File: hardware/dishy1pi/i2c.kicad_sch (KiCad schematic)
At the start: 19 parts, among them CN4 KF2EDGR-2.54-4P, CN5 KF2EDGR-2.54-4P, U6 LTC4311ISC6#TRPBF, U7 ISO1540DR, U8 LM75BIMX-5/NOPB

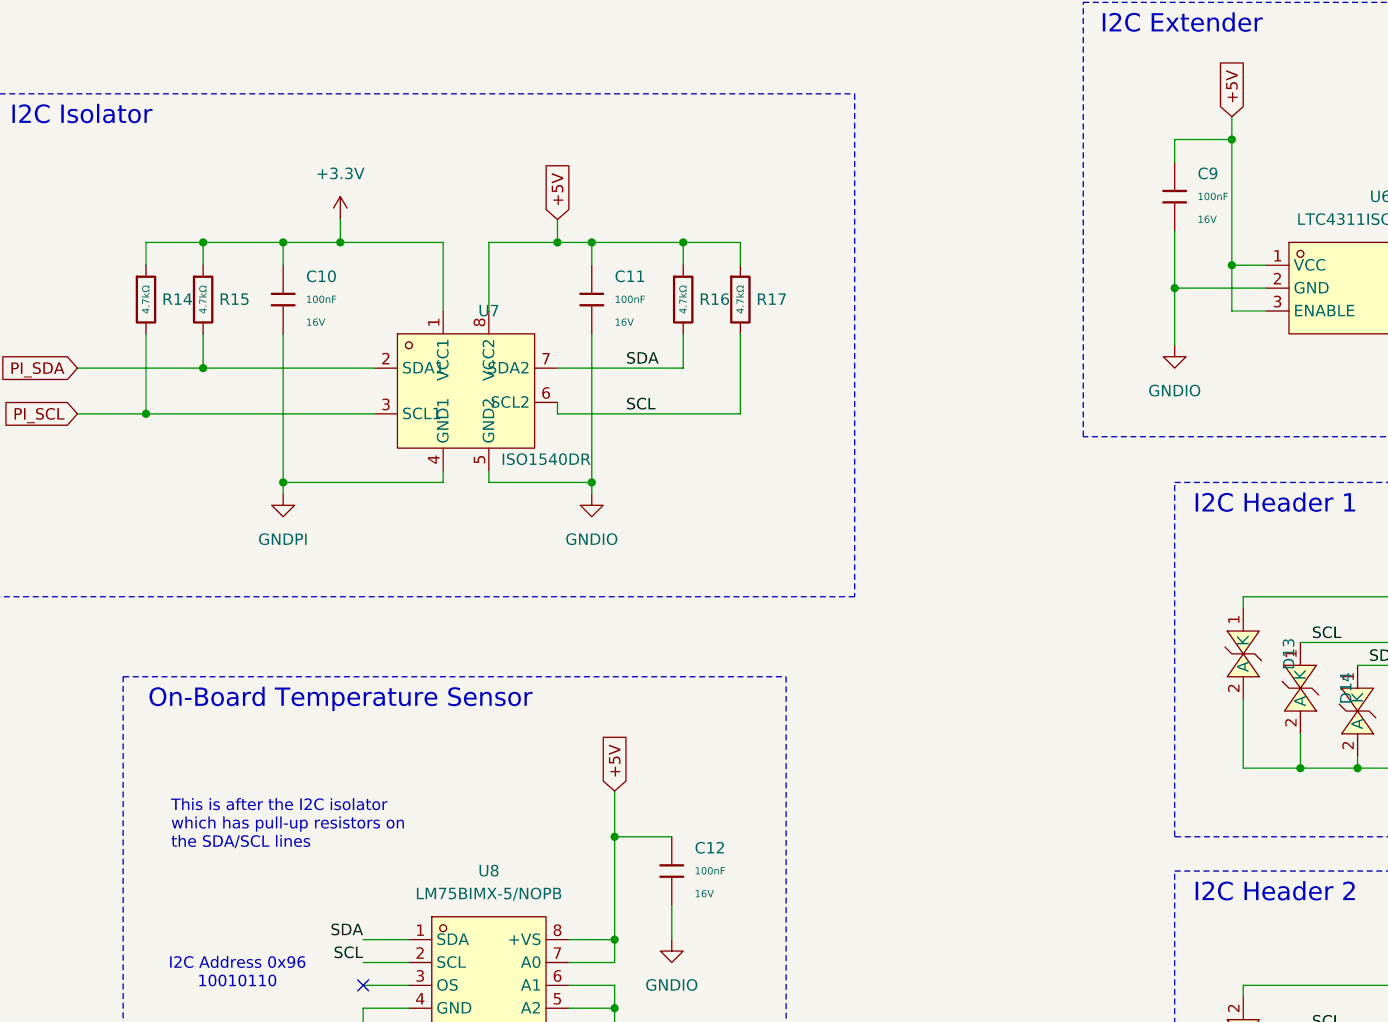
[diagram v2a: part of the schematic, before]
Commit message: Modifications based on first board assembly
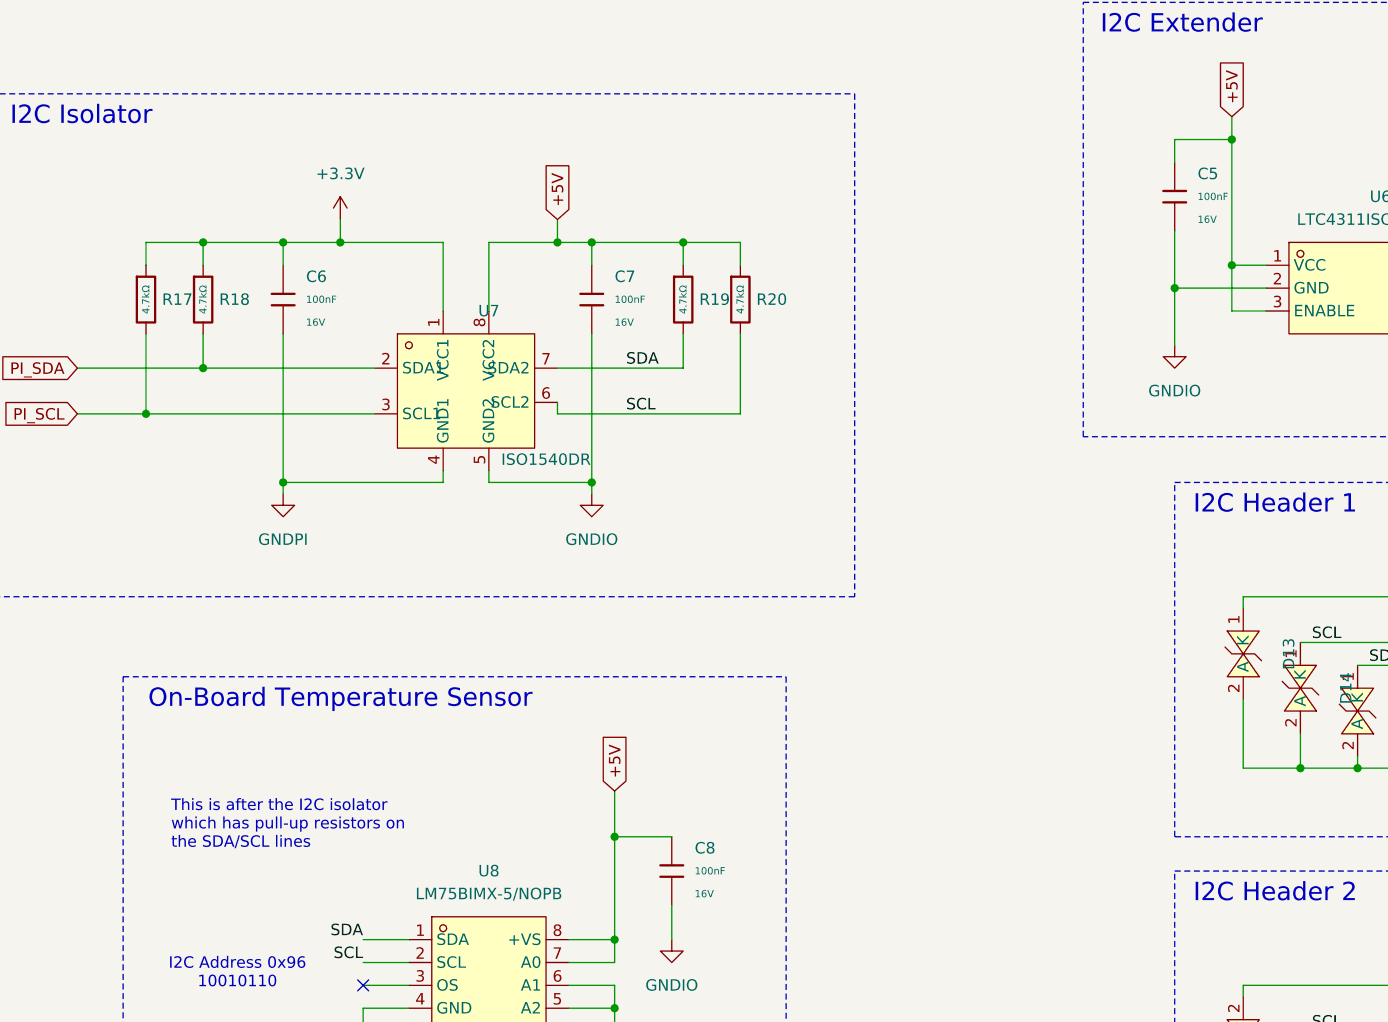
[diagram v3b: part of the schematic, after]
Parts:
- renumbered C9 to C5, C10 to C6, C11 to C7, C12 to C8, R14 to R17, R15 to R18, R16 to R19, R17 to R20
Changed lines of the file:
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@@
 		(title "I2C")
 		(date "2025-09-28")
-		(rev "1.1")
+		(rev "1.2")
 		(company "JRDish")
 		(comment 1 "I2C Circuits")
@@
 		(dnp no)
 		(fields_autoplaced yes)
-		(property "Reference" "C12"
+		(property "Reference" "C8"
 			(at 116.84 120.6499 0)
 			(effects
@@
 			(project ""
 				(path "/e63e39d7-6ac0-4ffd-8aa3-1841a4541b55/2849b2fb-7367-47ef-9d93-b400c9666642"
-					(reference "C12")
+					(reference "C8")
 					(unit 1)
 				)
@@
 		(on_board yes)
 		(dnp no)
-		(property "Reference" "R15"
+		(property "Reference" "R18"
 			(at 64.008 59.69 0)
 			(effects
@@
 			(project "DishyPi1"
 				(path "/e63e39d7-6ac0-4ffd-8aa3-1841a4541b55/2849b2fb-7367-47ef-9d93-b400c9666642"
-					(reference "R15")
+					(reference "R18")
 					(unit 1)
 				)
@@
 		(dnp no)
 		(fields_autoplaced yes)
-		(property "Reference" "#PWR25"
+		(property "Reference" "#PWR023"
 			(at 114.3 137.16 0)
 			(effects
@@
 			(project "DishyPi1"
 				(path "/e63e39d7-6ac0-4ffd-8aa3-1841a4541b55/2849b2fb-7367-47ef-9d93-b400c9666642"
-					(reference "#PWR25")
+					(reference "#PWR023")
 					(unit 1)
 				)
@@
 		(dnp no)
 		(fields_autoplaced yes)
-		(property "Reference" "#PWR23"
+		(property "Reference" "#PWR021"
 			(at 105.41 87.63 0)
 			(effects
@@
 			(project ""
 				(path "/e63e39d7-6ac0-4ffd-8aa3-1841a4541b55/2849b2fb-7367-47ef-9d93-b400c9666642"
-					(reference "#PWR23")
+					(reference "#PWR021")
 					(unit 1)
 				)
@@
 		(dnp no)
 		(fields_autoplaced yes)
-		(property "Reference" "C9"
+		(property "Reference" "C5"
 			(at 172.72 45.7199 0)
 			(effects
@@
 			(project "DishyPi1"
 				(path "/e63e39d7-6ac0-4ffd-8aa3-1841a4541b55/2849b2fb-7367-47ef-9d93-b400c9666642"
-					(reference "C9")
+					(reference "C5")
 					(unit 1)
 				)
@@
 		(dnp no)
 		(fields_autoplaced yes)
-		(property "Reference" "#PWR21"
+		(property "Reference" "#PWR019"
 			(at 208.28 71.12 0)
 			(effects
@@
 			(project "DishyPi1"
 				(path "/e63e39d7-6ac0-4ffd-8aa3-1841a4541b55/2849b2fb-7367-47ef-9d93-b400c9666642"
-					(reference "#PWR21")
+					(reference "#PWR019")
 					(unit 1)
 				)
@@
 		(dnp no)
 		(fields_autoplaced yes)
-		(property "Reference" "#PWR19"
+		(property "Reference" "#PWR017"
 			(at 77.47 54.61 0)
 			(effects
@@
 			(project ""
 				(path "/e63e39d7-6ac0-4ffd-8aa3-1841a4541b55/2849b2fb-7367-47ef-9d93-b400c9666642"
-					(reference "#PWR19")
+					(reference "#PWR017")
 					(unit 1)
 				)
@@
 		(on_board yes)
 		(dnp no)
-		(property "Reference" "R14"
+		(property "Reference" "R17"
 			(at 57.658 59.69 0)
 			(effects
@@
 			(project "DishyPi1"
 				(path "/e63e39d7-6ac0-4ffd-8aa3-1841a4541b55/2849b2fb-7367-47ef-9d93-b400c9666642"
-					(reference "R14")
+					(reference "R17")
 					(unit 1)
 				)
@@
 		(on_board yes)
 		(dnp no)
-		(property "Reference" "#PWR24"
+		(property "Reference" "#PWR022"
 			(at 196.85 119.38 0)
 			(effects
@@
 			(project ""
 				(path "/e63e39d7-6ac0-4ffd-8aa3-1841a4541b55/2849b2fb-7367-47ef-9d93-b400c9666642"
-					(reference "#PWR24")
+					(reference "#PWR022")
 					(unit 1)
 				)
@@
 		(dnp no)
 		(fields_autoplaced yes)
-		(property "Reference" "#PWR20"
+		(property "Reference" "#PWR018"
 			(at 170.18 71.12 0)
 			(effects
@@
 			(project "DishyPi1"
 				(path "/e63e39d7-6ac0-4ffd-8aa3-1841a4541b55/2849b2fb-7367-47ef-9d93-b400c9666642"
-					(reference "#PWR20")
+					(reference "#PWR018")
 					(unit 1)
 				)
@@
 		(on_board yes)
 		(dnp no)
-		(property "Reference" "R17"
+		(property "Reference" "R20"
 			(at 123.698 59.69 0)
 			(effects
@@
 			(project "DishyPi1"
 				(path "/e63e39d7-6ac0-4ffd-8aa3-1841a4541b55/2849b2fb-7367-47ef-9d93-b400c9666642"
-					(reference "R17")
+					(reference "R20")
 					(unit 1)
 				)
@@
 		(dnp no)
 		(fields_autoplaced yes)
-		(property "Reference" "C10"
+		(property "Reference" "C6"
 			(at 73.66 57.1499 0)
 			(effects
@@
 			(project ""
 				(path "/e63e39d7-6ac0-4ffd-8aa3-1841a4541b55/2849b2fb-7367-47ef-9d93-b400c9666642"
-					(reference "C10")
+					(reference "C6")
 					(unit 1)
 				)
@@
 		(on_board yes)
 		(dnp no)
-		(property "Reference" "R16"
+		(property "Reference" "R19"
 			(at 117.348 59.69 0)
 			(effects
@@
 			(project ""
 				(path "/e63e39d7-6ac0-4ffd-8aa3-1841a4541b55/2849b2fb-7367-47ef-9d93-b400c9666642"
-					(reference "R16")
+					(reference "R19")
 					(unit 1)
 				)
@@
 		(dnp no)
 		(fields_autoplaced yes)
-		(property "Reference" "#PWR22"
+		(property "Reference" "#PWR020"
 			(at 71.12 87.63 0)
 			(effects
@@
 			(project ""
 				(path "/e63e39d7-6ac0-4ffd-8aa3-1841a4541b55/2849b2fb-7367-47ef-9d93-b400c9666642"
-					(reference "#PWR22")
+					(reference "#PWR020")
 					(unit 1)
 				)
@@
 		(dnp no)
 		(fields_autoplaced yes)
-		(property "Reference" "C11"
+		(property "Reference" "C7"
 			(at 107.95 57.1499 0)
 			(effects
@@
 			(project "DishyPi1"
 				(path "/e63e39d7-6ac0-4ffd-8aa3-1841a4541b55/2849b2fb-7367-47ef-9d93-b400c9666642"
-					(reference "C11")
+					(reference "C7")
 					(unit 1)
 				)
@@
 		(on_board yes)
 		(dnp no)
-		(property "Reference" "#PWR27"
+		(property "Reference" "#PWR025"
 			(at 196.85 162.56 0)
 			(effects
@@
 			(project "DishyPi1"
 				(path "/e63e39d7-6ac0-4ffd-8aa3-1841a4541b55/2849b2fb-7367-47ef-9d93-b400c9666642"
-					(reference "#PWR27")
+					(reference "#PWR025")
 					(unit 1)
 				)
@@
 		(dnp no)
 		(fields_autoplaced yes)
-		(property "Reference" "#PWR26"
+		(property "Reference" "#PWR024"
 			(at 93.98 156.21 0)
 			(effects
@@
 			(project "DishyPi1"
 				(path "/e63e39d7-6ac0-4ffd-8aa3-1841a4541b55/2849b2fb-7367-47ef-9d93-b400c9666642"
-					(reference "#PWR26")
+					(reference "#PWR024")
 					(unit 1)
 				)

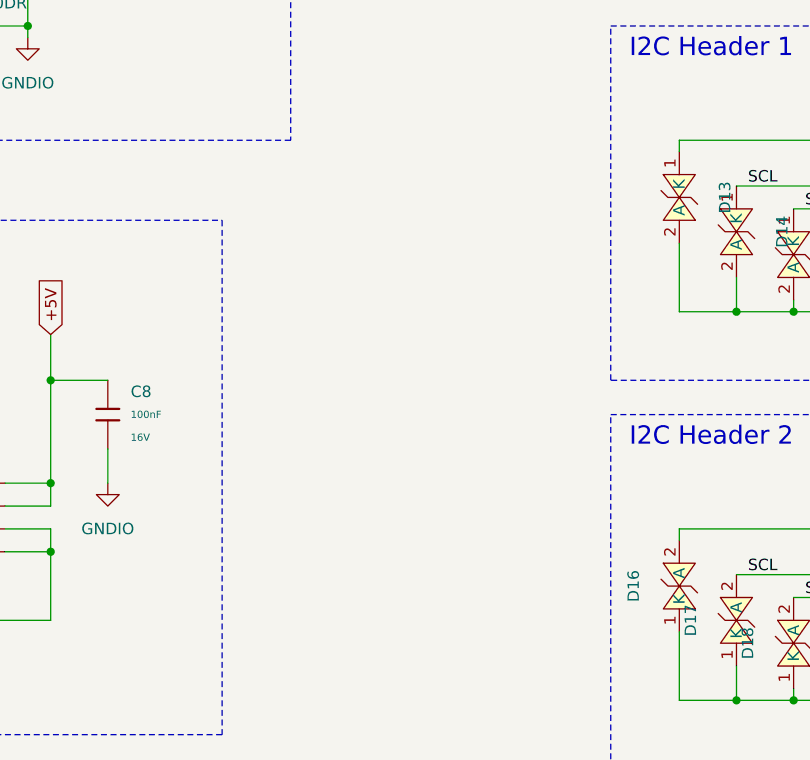
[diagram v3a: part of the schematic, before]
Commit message: Added power circuit to dishy schematic
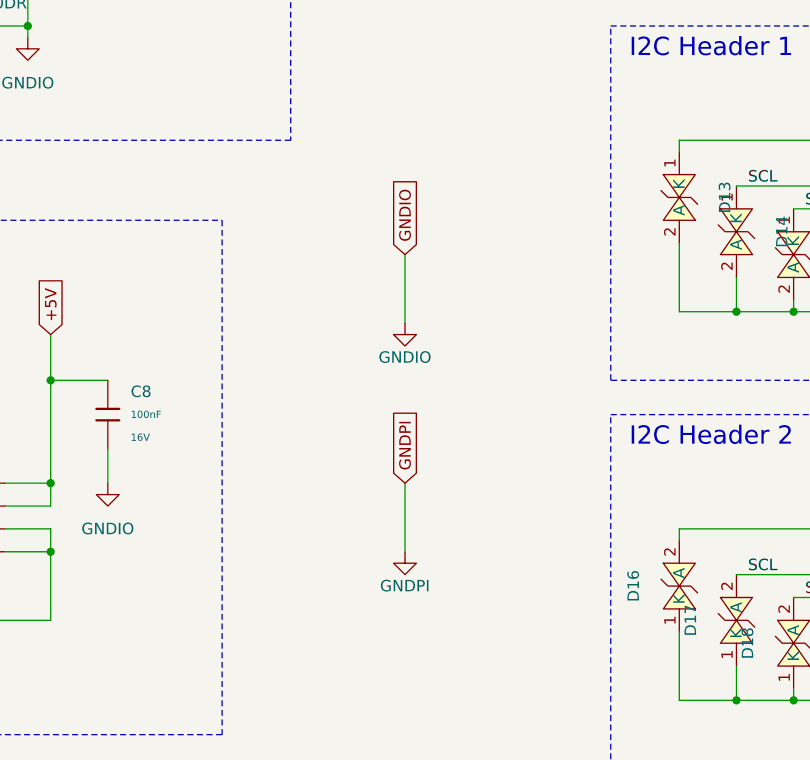
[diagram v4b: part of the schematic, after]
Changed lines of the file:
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@@
 	(wire
 		(pts
+			(xy 147.32 130.81) (xy 147.32 138.43)
+		)
+		(stroke
+			(width 0)
+			(type default)
+		)
+	)
+	(wire
+		(pts
 			(xy 93.98 146.05) (xy 93.98 149.86)
 		)
@@
 	(wire
 		(pts
+			(xy 147.32 105.41) (xy 147.32 113.03)
+		)
+		(stroke
+			(width 0)
+			(type default)
+		)
+	)
+	(wire
+		(pts
 			(xy 48.26 72.39) (xy 55.88 72.39)
 		)
@@
 		)
 	)
+	(global_label "GNDPI"
+		(shape input)
+		(at 147.32 130.81 90)
+		(fields_autoplaced yes)
+		(effects
+			(font
+				(size 1.27 1.27)
+			)
+			(justify left)
+		)
+		(property "Intersheetrefs" "${INTERSHEET_REFS}"
+			(at 147.32 121.9844 90)
+			(effects
+				(font
+					(size 1.27 1.27)
+				)
+				(justify left)
+				(hide yes)
+			)
+		)
+	)
 	(global_label "+5V"
 		(shape input)
@@
 		)
 	)
+	(global_label "GNDIO"
+		(shape input)
+		(at 147.32 105.41 90)
+		(fields_autoplaced yes)
+		(effects
+			(font
+				(size 1.27 1.27)
+			)
+			(justify left)
+		)
+		(property "Intersheetrefs" "${INTERSHEET_REFS}"
+			(at 147.32 96.5239 90)
+			(effects
+				(font
+					(size 1.27 1.27)
+				)
+				(justify left)
+				(hide yes)
+			)
+		)
+	)
 	(global_label "PI_SCL"
 		(shape input)
@@
 	)
 	(symbol
+		(lib_id "power:GND")
+		(at 147.32 113.03 0)
+		(unit 1)
+		(exclude_from_sim no)
+		(in_bom yes)
+		(on_board yes)
+		(dnp no)
+		(property "Reference" "#PWR040"
+			(at 147.32 119.38 0)
+			(effects
+				(font
+					(size 1.27 1.27)
+				)
+				(hide yes)
+			)
+		)
+		(property "Value" "GNDIO"
+			(at 147.32 116.84 0)
+			(effects
+				(font
+					(size 1.27 1.27)
+				)
+			)
+		)
+		(property "Footprint" ""
+			(at 147.32 113.03 0)
+			(effects
+				(font
+					(size 1.27 1.27)
+				)
+				(hide yes)
+			)
+		)
+		(property "Datasheet" ""
+			(at 147.32 113.03 0)
+			(effects
+				(font
+					(size 1.27 1.27)
+				)
+				(hide yes)
+			)
+		)
+		(property "Description" "Power symbol creates a global label with name \"GND\" , ground"
+			(at 147.32 113.03 0)
+			(effects
+				(font
+					(size 1.27 1.27)
+				)
+				(hide yes)
+			)
+		)
+		(pin "1"
+		)
+		(instances
+			(project "DishyPi1"
+				(path "/e63e39d7-6ac0-4ffd-8aa3-1841a4541b55/2849b2fb-7367-47ef-9d93-b400c9666642"
+					(reference "#PWR040")
+					(unit 1)
+				)
+			)
+		)
+	)
+	(symbol
 		(lib_id "PCM_JLCPCB-Capacitors:0402,100nF")
 		(at 105.41 59.69 0)
@@
 					(unit 1)
 				)
+			)
+		)
+	)
+	(symbol
+		(lib_id "power:GND")
+		(at 147.32 138.43 0)
+		(unit 1)
+		(exclude_from_sim no)
+		(in_bom yes)
+		(on_board yes)
+		(dnp no)
+		(property "Reference" "#PWR041"
+			(at 147.32 144.78 0)
+			(effects
+				(font
+					(size 1.27 1.27)
+				)
+				(hide yes)
+			)
+		)
+		(property "Value" "GNDPI"
+			(at 147.32 142.24 0)
+			(effects
+				(font
+					(size 1.27 1.27)
+				)
+			)
+		)
+		(property "Footprint" ""
+			(at 147.32 138.43 0)
+			(effects
+				(font
+					(size 1.27 1.27)
+				)
+				(hide yes)
+			)
+		)
+		(property "Datasheet" ""
+			(at 147.32 138.43 0)
+			(effects
+				(font
+					(size 1.27 1.27)
+				)
+				(hide yes)
+			)
+		)
+		(property "Description" "Power symbol creates a global label with name \"GND\" , ground"
+			(at 147.32 138.43 0)
+			(effects
+				(font
+					(size 1.27 1.27)
+				)
+				(hide yes)
+			)
+		)
+		(pin "1"
+		)
+		(instances
+			(project "DishyPi1"
+				(path "/e63e39d7-6ac0-4ffd-8aa3-1841a4541b55/2849b2fb-7367-47ef-9d93-b400c9666642"
+					(reference "#PWR041")
+					(unit 1)
+				)
